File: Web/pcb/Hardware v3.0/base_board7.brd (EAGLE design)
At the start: 80.3 x 80.3 mm, 143 parts, among them IC1 LM2596S, IC2A TDA2822D, IC2B LM386M-1, IC3 TJA1040T, IC4 STM32F103RBT6, IC5 MIC2288BML, IC6 ULN2003AD, IC7 LM2901M, IC8 REG1117, IC9A SN74LVC1G10DCKR, IC9B SN74HC10D, Q1 CSM-7X-DU

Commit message: software updates
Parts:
- added L5: (no value), resistor:TJ3-U1
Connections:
- net N$3: now also L5.1
- net VCC: now also L5.2
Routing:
- net N$3: track 18.5 -> 26.1 mm
- net VCC: track 56.3 -> 58.3 mm
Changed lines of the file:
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@@
 <attribute name="VALUE" x="20.7264" y="0.4476" size="0.0254" layer="27"/>
+</element>
+<element name="L5" library="resistor" library_urn="urn:adsk.eagle:library:348" package="TJ3-U1" package3d_urn="urn:adsk.eagle:package:23496/1" value="" x="-9.6012" y="31.8516" smashed="yes">
+<attribute name="NAME" x="-10.2362" y="26.7716" size="1.27" layer="25" rot="R90"/>
+<attribute name="VALUE" x="-7.6962" y="26.7716" size="1.27" layer="27" rot="R90"/>
 </element>
 </elements>
@@
 <wire x1="-23.5458" y1="31.8516" x2="-23.5458" y2="27.7778" width="0.8128" layer="1"/>
 <wire x1="-23.368" y1="27.6" x2="-23.5458" y2="27.7778" width="0.1524" layer="1"/>
+<contactref element="L5" pad="1"/>
+<wire x1="-12.9012" y1="31.8516" x2="-10.3632" y2="31.8516" width="0.8128" layer="1"/>
+<wire x1="-9.398" y1="30.8864" x2="-9.398" y2="27.154" width="0.8128" layer="1"/>
+<wire x1="-10.3632" y1="31.8516" x2="-9.398" y2="30.8864" width="0.8128" layer="1"/>
 </signal>
 <signal name="VCC">
@@
 <contactref element="IC3" pad="3"/>
 <contactref element="L2" pad="1"/>
-<wire x1="-1.5" y1="28.956" x2="-9.398" y2="36.854" width="0.8128" layer="1"/>
+<wire x1="-1.5" y1="28.956" x2="-4.3314" y2="31.7874" width="0.8128" layer="1"/>
+<wire x1="-4.3314" y1="31.7874" x2="-9.398" y2="36.854" width="0.8128" layer="1"/>
 <wire x1="-23.81" y1="-30.51" x2="-26.499" y2="-30.51" width="0.1524" layer="1"/>
 <wire x1="-26.67" y1="-30.339" x2="-26.499" y2="-30.51" width="0.1524" layer="1"/>
@@
 <wire x1="-17.288" y1="-30.21" x2="-17.272" y2="-30.226" width="0.1524" layer="1"/>
 <wire x1="0.762" y1="28.956" x2="0.762" y2="31.336" width="0.6096" layer="1"/>
+<contactref element="L5" pad="2"/>
+<wire x1="-6.3012" y1="31.8516" x2="-4.3956" y2="31.8516" width="0.8128" layer="1"/>
+<wire x1="-4.3956" y1="31.8516" x2="-4.3314" y2="31.7874" width="0.1524" layer="1"/>
 </signal>
 <signal name="N$4">

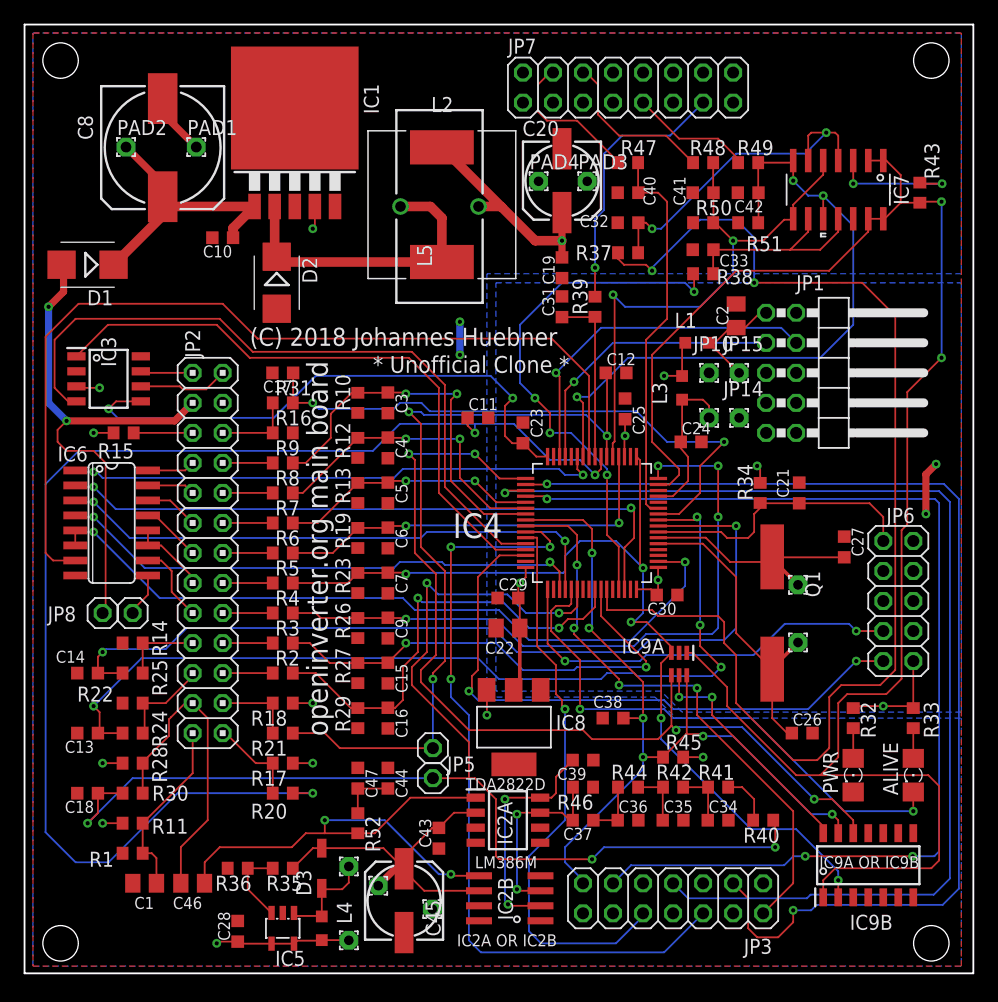
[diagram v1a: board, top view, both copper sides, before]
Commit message: swd over esp progress
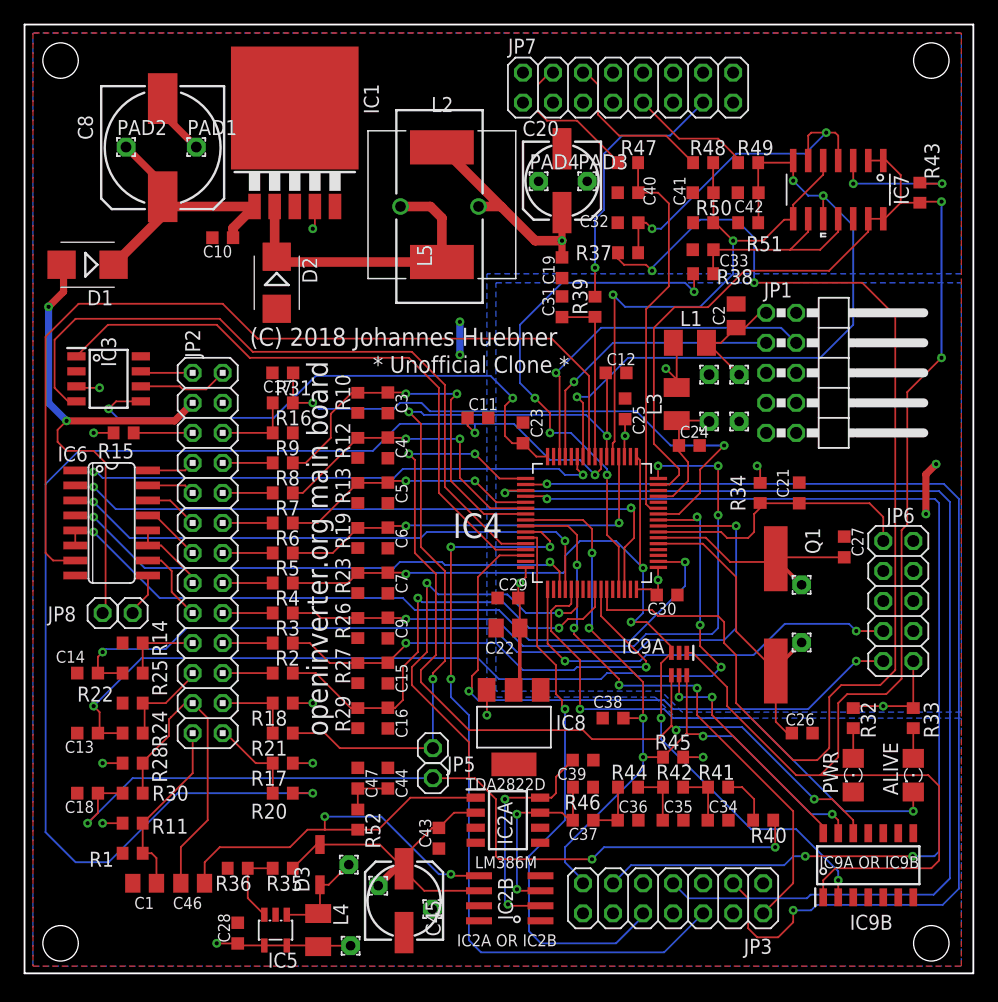
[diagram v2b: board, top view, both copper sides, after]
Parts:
- L1, L3, L4: device rcl:L2012C -> rcl:L3225M
- moved L3 1.45 mm to (10.5, 15.1)
- moved IC5 0.63 mm to (-23.5, -29.4)
- moved L1 0.61 mm to (11.6, 20.3)
- moved JP12 0.48 mm to (-17.1, -30.7)
- moved C24 0.34 mm to (11.5, 11.6)
- moved D3 0.34 mm to (-19.7, -23.8)
- moved L4 0.34 mm to (-19.9, -29.4)
- moved Q1 0.34 mm to (18.8, -2.69)
- moved JP11 0.30 mm to (13.2, 13.7)
- moved JP14 0.30 mm to (15.7, 13.7)
- moved R52 0.30 mm to (-16.5, -20.0)
- moved JP16 0.30 mm to (21.0, -5.03)
- moved JP17 0.30 mm to (21.0, -0.15)
- moved C28 0.15 mm to (-26.7, -29.6)
- moved JP10 0.15 mm to (13.2, 17.6)
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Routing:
- net N$8: track 13.7 -> 11.3 mm
- net VCCIO: track 105.7 -> 107.1 mm
- net PA1/TIM2_CH2: track 149.2 -> 150.3 mm

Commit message: some pcb optimizations
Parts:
- added TP1: TPB1,27, testpad:B1,27
- ALIVE, PWR: device eagle-ltspice:LED_1206 -> led:SML0805
- turned ALIVE to 90 degrees
- turned PWR to 90 degrees

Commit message: board test confirmed
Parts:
- moved ALIVE 0.76 mm to (30.5, -15.5)
- moved PWR 0.76 mm to (25.4, -15.5)
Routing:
- net PB7/TIM4_CH2: track 102.4 -> 107.7 mm
- net PA1/TIM2_CH2: track 150.4 -> 155.2 mm
- net VCCIO: track 107.1 -> 103.3 mm
- net PC12: track 45.8 -> 43.3 mm
- net PB12/TIM1_BKIN: track 79.5 -> 80.3 mm
- net N$5: track 2.93 -> 2.16 mm
- net N$2: track 2.93 -> 2.16 mm
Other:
- board text added: "+"

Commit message: ui updates
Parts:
- moved R15 0.15 mm to (-36.3, 12.5)
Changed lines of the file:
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@@
 <attribute name="VALUE" x="-7.15" y="12.32" size="1.016" layer="27"/>
 </element>
-<element name="R15" library="rcl" library_urn="urn:adsk.eagle:library:334" package="R0603" package3d_urn="urn:adsk.eagle:package:23555/2" value="510" x="-36.322" y="12.7" smashed="yes" rot="R180">
+<element name="R15" library="rcl" library_urn="urn:adsk.eagle:library:334" package="R0603" package3d_urn="urn:adsk.eagle:package:23555/2" value="510" x="-36.322" y="12.5476" smashed="yes" rot="R180">
 <attribute name="NAME" x="-35.433" y="11.811" size="1.27" layer="25" rot="R180"/>
-<attribute name="SPICEPREFIX" value="R" x="-36.322" y="12.7" size="1.778" layer="27" rot="R180" display="off"/>
-<attribute name="VALUE" x="-35.687" y="14.605" size="1.27" layer="27" rot="R180"/>
+<attribute name="SPICEPREFIX" value="R" x="-36.322" y="12.5476" size="1.778" layer="27" rot="R180" display="off"/>
+<attribute name="VALUE" x="-35.687" y="14.4526" size="1.27" layer="27" rot="R180"/>
 </element>
 <element name="R31" library="rcl" library_urn="urn:adsk.eagle:library:334" package="R0603" package3d_urn="urn:adsk.eagle:package:23555/2" value="10k" x="-22.86" y="15.24" smashed="yes">
@@
 <wire x1="-20.32" y1="-15.24" x2="-22.01" y2="-15.24" width="0.1524" layer="1"/>
 <via x="-38.862" y="12.7" extent="1-16" drill="0.35"/>
-<wire x1="-37.172" y1="12.7" x2="-38.862" y2="12.7" width="0.1524" layer="1"/>
+<wire x1="-37.172" y1="12.5476" x2="-38.7096" y2="12.5476" width="0.1524" layer="1"/>
+<wire x1="-38.7096" y1="12.5476" x2="-38.862" y2="12.7" width="0.1524" layer="1"/>
 <via x="-38.354" y="16.51" extent="1-16" drill="0.35"/>
 <wire x1="-38.354" y1="16.51" x2="-40.19" y2="16.51" width="0.1524" layer="1"/>
@@
 <contactref element="JP2" pad="22"/>
 <contactref element="R15" pad="1"/>
-<wire x1="-35.472" y1="12.7" x2="-30.48" y2="12.7" width="0.1524" layer="1"/>
+<wire x1="-30.6324" y1="12.5476" x2="-30.48" y2="12.7" width="0.1524" layer="1"/>
+<wire x1="-30.6324" y1="12.5476" x2="-35.472" y2="12.5476" width="0.1524" layer="1"/>
 </signal>
 <signal name="CANH">

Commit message: updates
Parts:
- moved R43 0.30 mm to (30.7, 33.0)
- moved C25 0.25 mm to (6.35, 14.7)
- moved C30 0.15 mm to (9.65, -1.17)
- moved JP17 0.15 mm to (21.0, -0.30)
- moved JP16 0.05 mm to (21.0, -5.08)
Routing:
- net PA10/TIM1_CH3: track 47.8 -> 47.0 mm
- net PA3/ADC3: track 82.0 -> 81.3 mm
- net VCC: track 58.4 -> 57.7 mm
